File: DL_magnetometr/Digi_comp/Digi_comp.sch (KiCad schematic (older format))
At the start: 52 parts, among them J1 USB_B_Micro, U1 AP7331-WG-7, U2 74AHCT1G125, U3 JST-PHR-2, U4 AZ4558CM, U5 AZ4558CM, U6 AP7331-WG-7, Y1 32.768k, Y2 16M/32M

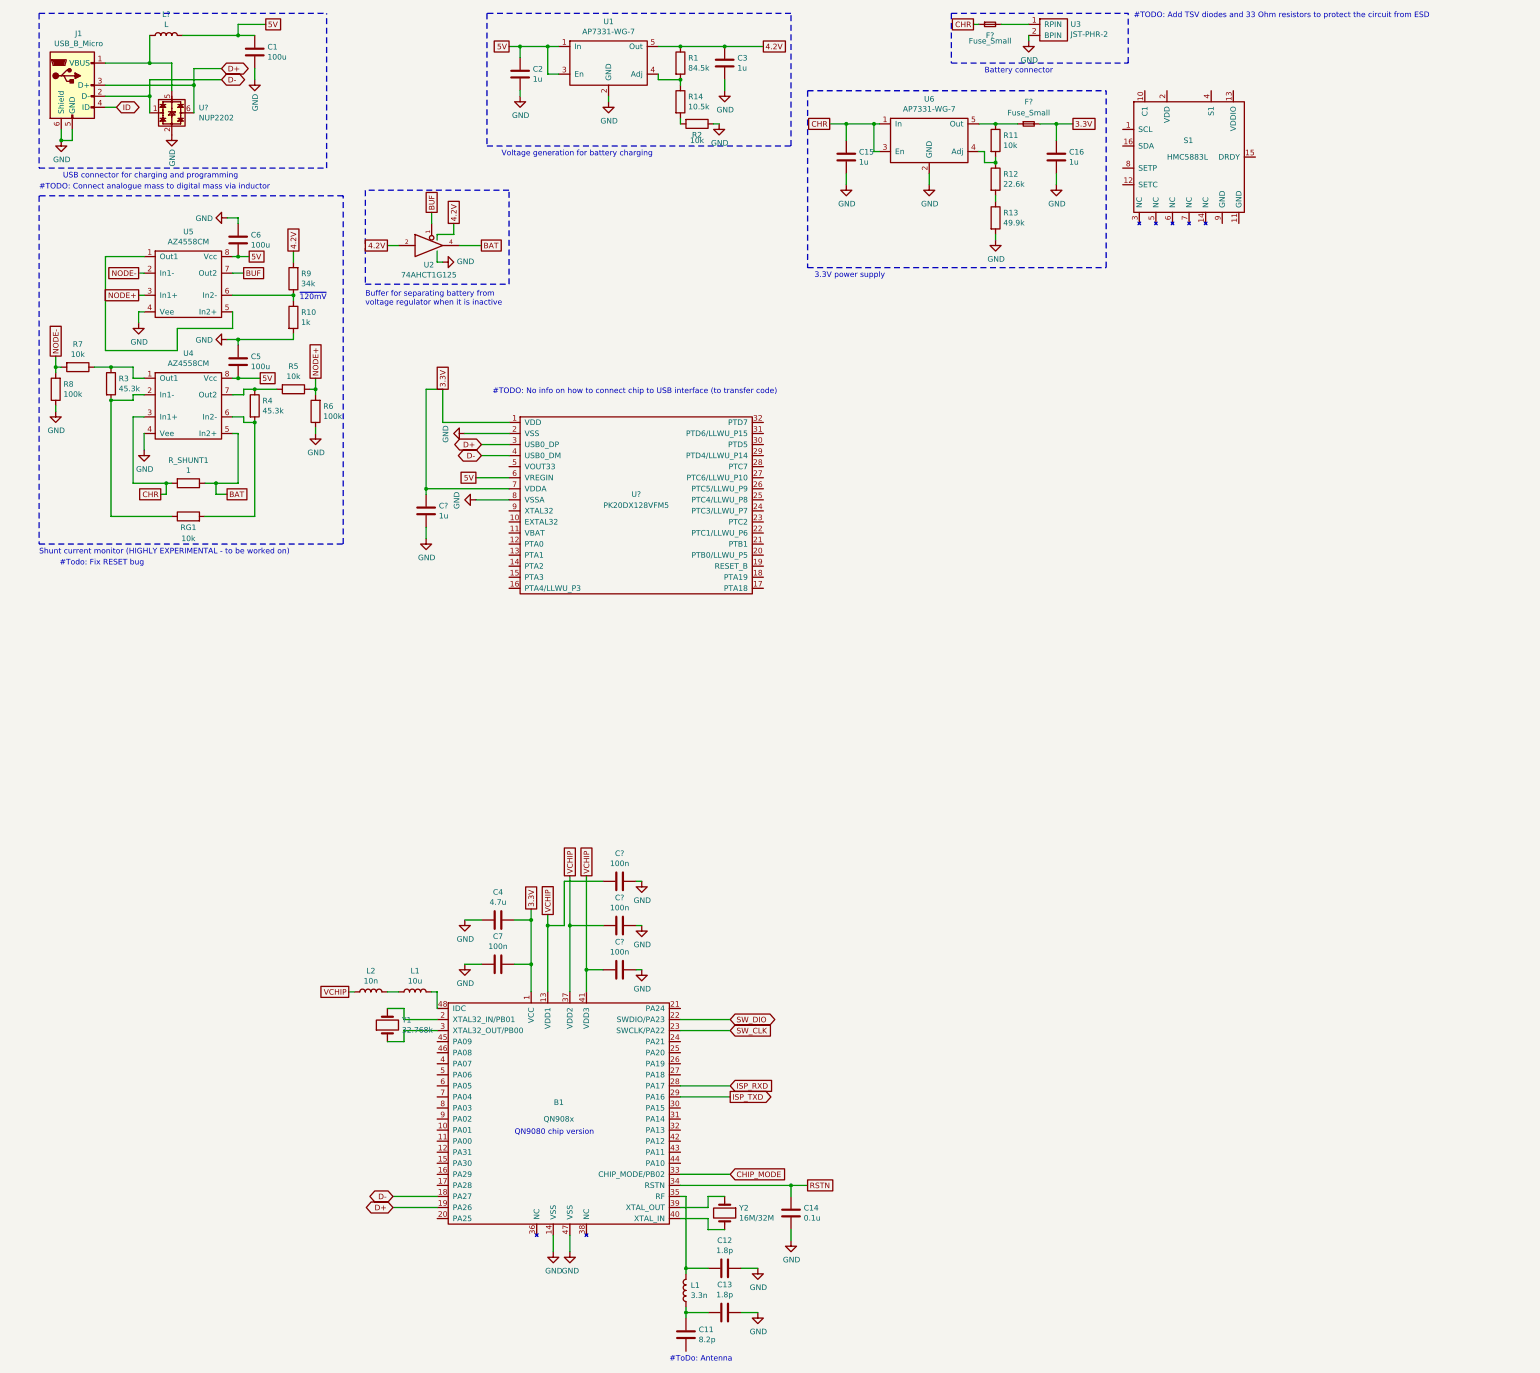
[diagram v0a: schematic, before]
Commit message: Added descriptions and changed placement for readability.
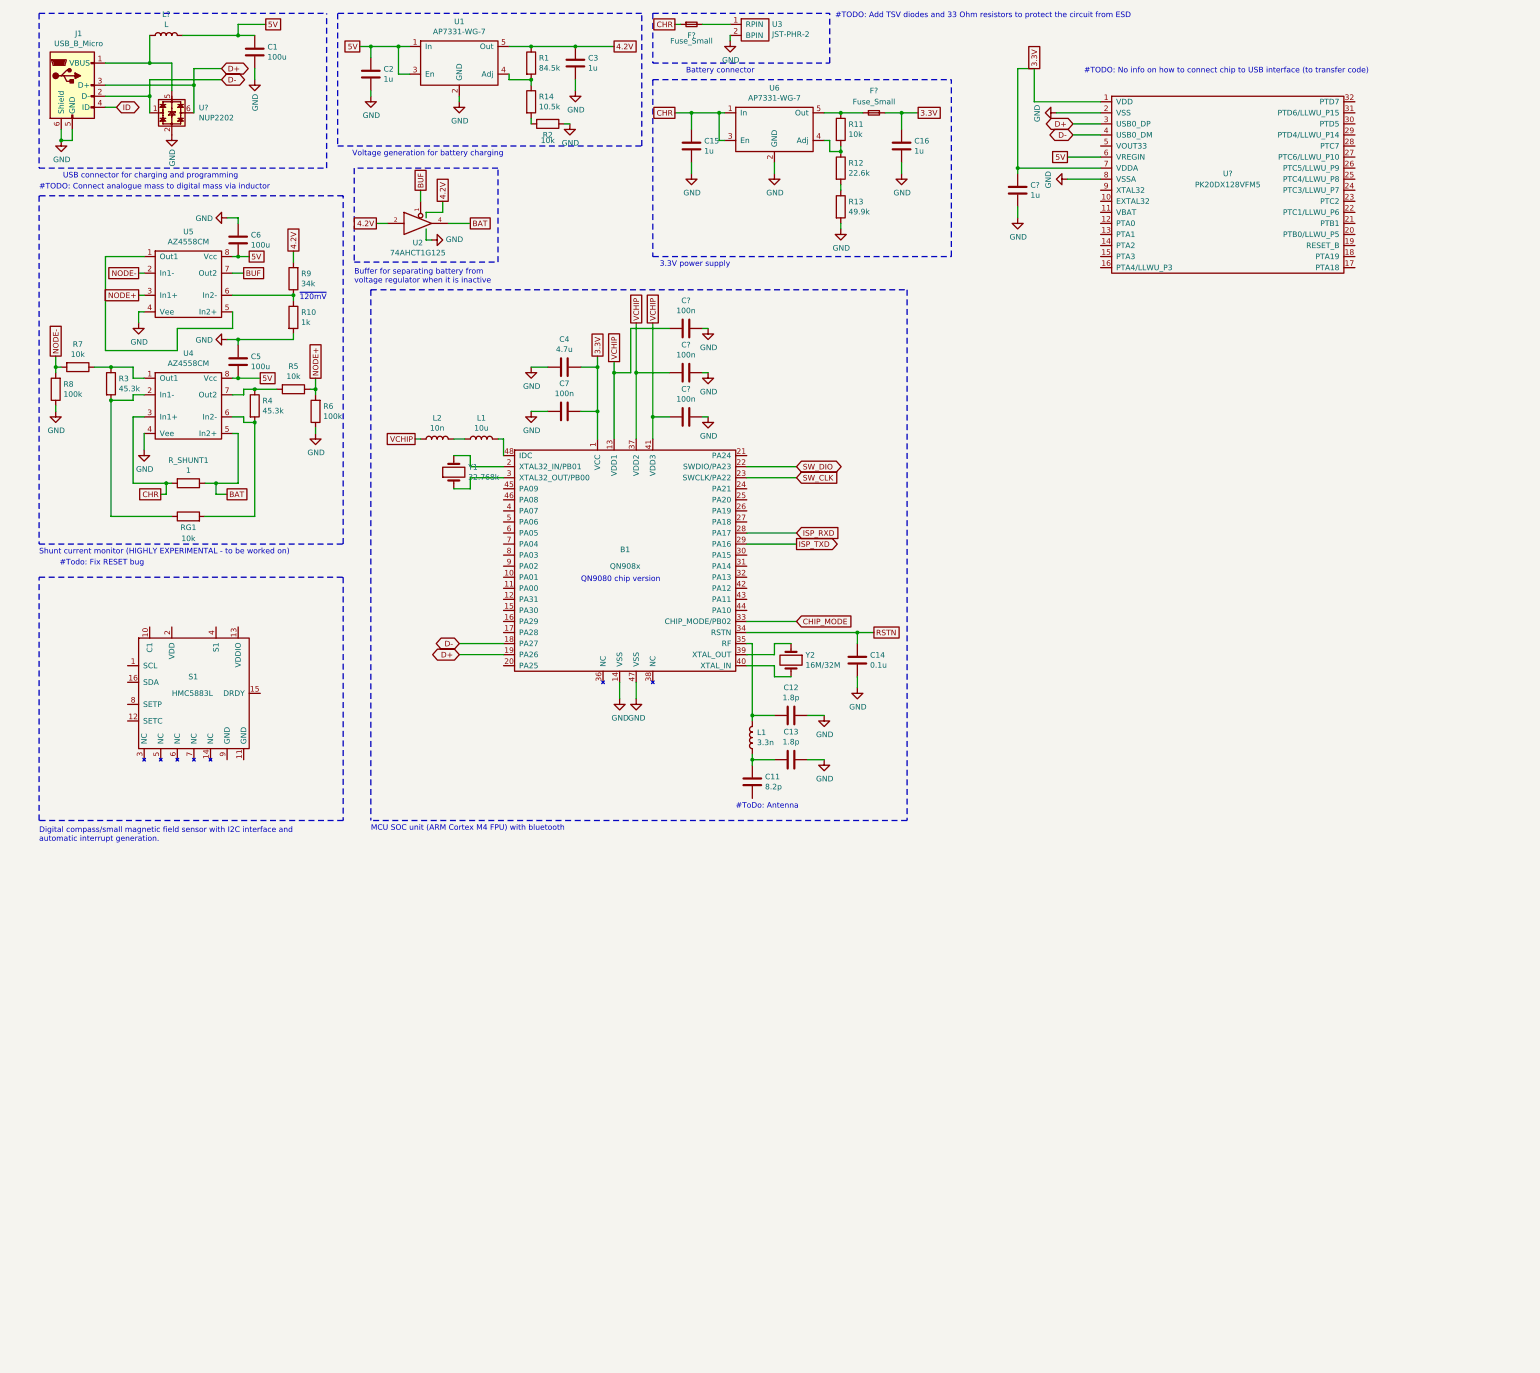
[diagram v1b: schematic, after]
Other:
- note added: "Digital compass/small magnetic field sensor with I2C interface and\nautomatic interrupt generation."
- note added: "MCU SOC unit (ARM Cortex M4 FPU) with bluetooth"
- moved on the sheet: B1, C11, C12, C13, C14, C15, C16, C2, C3, C4, C7, C?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

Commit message: Added comments.
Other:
- note added: "#TODO: Change to Schottky diode"
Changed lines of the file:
@@
 Text Notes 500  8050 0    50   ~ 0
 Digital compass/small magnetic field sensor with I2C interface and\nautomatic interrupt generation.
+Text Notes 4650 2350 0    50   ~ 0
+#TODO: Change to Schottky diode
 $EndSCHEMATC
